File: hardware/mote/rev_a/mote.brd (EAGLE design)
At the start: 160 x 100 mm, 71 parts, among them Q1 CSD22206W, Q2 CSD75207W15, Q3 CSD75207W15, Q4 CSD13303W1015, Q5 CSD22206W, U1 NRF52840, U10 MS5637-02BA03, U3 MAX17222, U4 TPS3839G25DBZ, U5 SI7021-A20-GM1, U6 ISL29125, U7 MAX44009, U8 LIS2DW12, U9 AB1815-T3, X1 7V-32.000MAHV-T, X3 ABS07-32.768KHZ-7-T

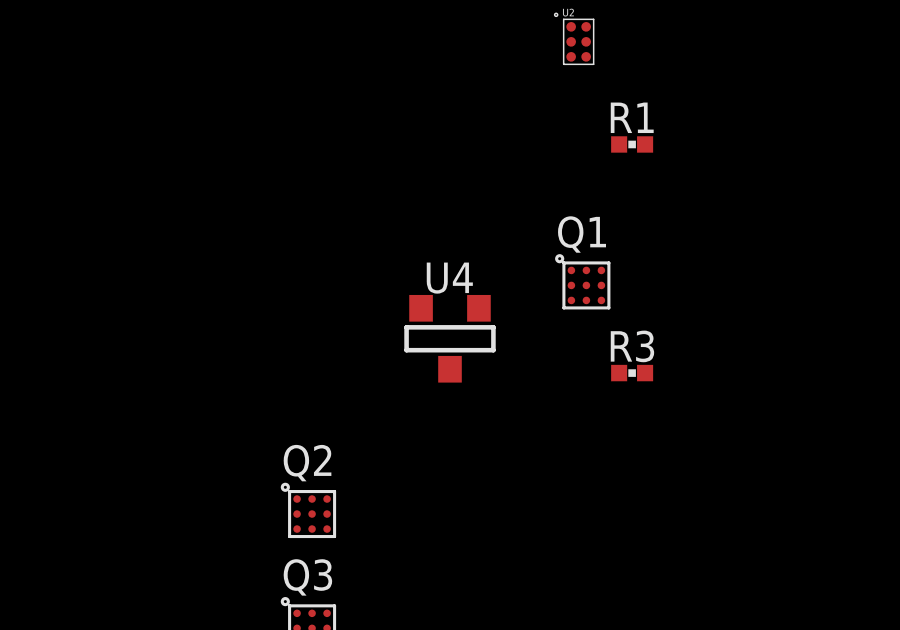
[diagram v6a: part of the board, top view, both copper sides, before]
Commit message: Do undervoltage check in software
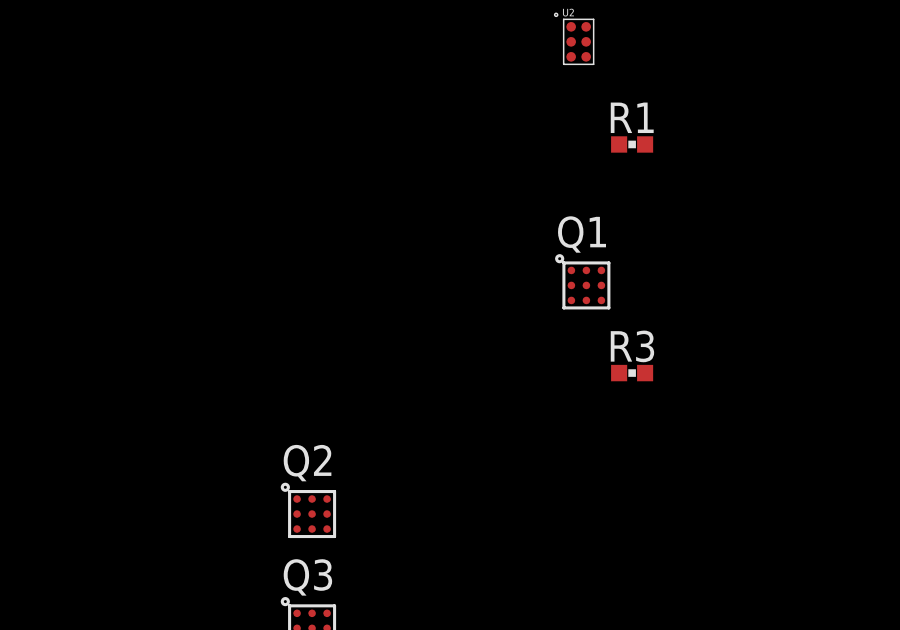
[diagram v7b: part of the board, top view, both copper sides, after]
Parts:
- removed U4: TPS3839G25DBZ, chips:SOT-23
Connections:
- removed net N$15: D3.A, Q4.A2, Q5.A1, R6.1, TP3.TESTPOINT, U4.2
- new net SRC_SW: D3.A, Q4.A2, Q5.A1, R6.1, TP3.TESTPOINT
- net GND: no longer U4.1
- net N$24: no longer U4.3
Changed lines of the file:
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@@
 " x="0.762" y="-40.513" size="1.778" layer="27" display="off"/>
-</element>
-<element name="U4" library="chips" package="SOT-23" value="TPS3839G25DBZ" x="-5.334" y="-39.37">
-<attribute name="DIGIKEY" value="296-42522-1-ND" x="-5.334" y="-39.37" size="1.778" layer="27" display="off"/>
-<attribute name="MANUFACTURER" value="TEXAS INSTRUMENTS" x="-5.334" y="-39.37" size="1.778" layer="27" display="off"/>
-<attribute name="MPN" value="TPS3839G25DBZR" x="-5.334" y="-39.37" size="1.778" layer="27" display="off"/>
 </element>
 <element name="Q2" library="fets" package="DSBGA" value="CSD75207W15" x="-9.906" y="-45.212">
@@
 <via x="33.147" y="21.717" extent="1-16" drill="0.762"/>
 <via x="26.797" y="15.621" extent="1-16" drill="0.762"/>
-<contactref element="U4" pad="1"/>
 <contactref element="Q4" pad="C2"/>
 <contactref element="Q4" pad="B2"/>
@@
 <wire x1="-9.402" y1="-53.332" x2="-70.525" y2="-89.4" width="0" layer="19" extent="1-1"/>
 <wire x1="-9.402" y1="-52.832" x2="-9.402" y2="-53.332" width="0" layer="19" extent="1-1"/>
-<wire x1="-4.3434" y1="-38.354" x2="-9.402" y2="-52.832" width="0" layer="19" extent="1-1"/>
-<wire x1="0.32893125" y1="-40.513" x2="-4.3434" y2="-38.354" width="0" layer="19" extent="1-1"/>
-<wire x1="-0.77" y1="-29.472" x2="-4.3434" y2="-38.354" width="0" layer="19" extent="1-1"/>
+<wire x1="0.32893125" y1="-40.513" x2="-9.402" y2="-52.832" width="0" layer="19" extent="1-1"/>
+<wire x1="-0.77" y1="-29.472" x2="0.32893125" y2="-40.513" width="0" layer="19" extent="1-1"/>
 <wire x1="-0.77" y1="-28.972" x2="-0.77" y2="-29.472" width="0" layer="19" extent="1-1"/>
 <wire x1="15.43" y1="-22.86" x2="-0.77" y2="-28.972" width="0" layer="19" extent="1-1"/>
@@
 <wire x1="-0.77" y1="-29.972" x2="0.32893125" y2="-32.893" width="0" layer="19" extent="1-1"/>
 </signal>
-<signal name="N$15">
-<contactref element="U4" pad="2"/>
+<signal name="SRC_SW">
 <contactref element="Q5" pad="A1"/>
 <contactref element="Q4" pad="A2"/>
@@
 <wire x1="-10.406" y1="-56.142" x2="-75.36306875" y2="-93.98" width="0" layer="19" extent="1-1"/>
 <wire x1="-9.402" y1="-52.332" x2="-10.406" y2="-56.142" width="0" layer="19" extent="1-1"/>
-<wire x1="-6.2738" y1="-38.354" x2="-9.402" y2="-52.332" width="0" layer="19" extent="1-1"/>
-<wire x1="-56.261" y1="61.722" x2="-6.2738" y2="-38.354" width="0" layer="19" extent="1-1"/>
+<wire x1="-56.261" y1="61.722" x2="-9.402" y2="-52.332" width="0" layer="19" extent="1-1"/>
 </signal>
 <signal name="N$17">
@@
 <contactref element="Q1" pad="C2"/>
 <contactref element="Q1" pad="C3"/>
-<contactref element="U4" pad="3"/>
 <contactref element="TP1" pad="TESTPOINT"/>
 <contactref element="Q5" pad="A2"/>
@@
 <wire x1="-9.406" y1="-44.712" x2="-9.406" y2="-45.212" width="0" layer="19" extent="1-1"/>
 <wire x1="-9.906" y1="-44.712" x2="-9.406" y2="-44.712" width="0" layer="19" extent="1-1"/>
-<wire x1="-5.3086" y1="-40.386" x2="-9.406" y2="-44.712" width="0" layer="19" extent="1-1"/>
-<wire x1="-1.262" y1="-38.092" x2="-5.3086" y2="-40.386" width="0" layer="19" extent="1-1"/>
+<wire x1="-1.262" y1="-38.092" x2="-9.406" y2="-44.712" width="0" layer="19" extent="1-1"/>
 <wire x1="-0.762" y1="-38.092" x2="-1.262" y2="-38.092" width="0" layer="19" extent="1-1"/>
 <wire x1="-0.262" y1="-38.092" x2="-0.762" y2="-38.092" width="0" layer="19" extent="1-1"/>

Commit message: Connect all gpio, add pir
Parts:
- added J1: TC2030-JLINK-L, connector:TC2030-IDC
- added JP1, JP2, JP3, JP4, JP5, JP6, JP7, JP8: (no value), SparkFun-Passives:SJ_2S
- added Q10, Q11, Q6, Q7, Q8, Q9: CSD22206W, fets:DSBGA
- added R10, R11, R12, R13, R14, R9: 100MΩ, passives:0402_RES
- added TP12, TP13, TP14, TP15, TP16, TP17, TP18, TP19, TP20, TP21, TP22, TP23, TP24, TP25, TP26, TP27, TP28, TP29: TEST_POINT_0.040IN, headers:TESTPOINT_0.040IN
- added U4: AMN41121, chips:AMN2
- R1: value 1k -> 1kΩ
- R2: value 80.6k -> 80.6kΩ
- R3: value 20 -> 20Ω
- R4: value 33M -> 33MΩ
- R5, R6: value 100k -> 100kΩ
- R7, R8: value 10k -> 10kΩ
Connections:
- removed net !LGHT_INT: U7.4
- removed net ACL_CS: U8.2
- removed net ACL_INT1: U8.12
- removed net ACL_INT2: U8.11
- removed net CS_RTC: U9.12
- removed net ENABLE: R4.2
- removed net SW1: L3.P$2, TP11.TESTPOINT, U3.2
- new net !ACC_EN: Q6.A1, R9.1, U1.A14
- new net !CLR_EN: Q7.A1, R10.1, U1.B15
- new net !HUM_EN: Q10.A1, R13.1, U1.B19
- new net !LT_EN: Q8.A1, R11.1, U1.A16
- new net !LT_INT: U1.U24, U7.4
- new net !PIR_EN: Q11.A1, R14.1, U1.A20
- new net !PR_EN: Q9.A1, R12.1, U1.B17
- new net ACC_CS: U1.AD12, U8.2
- new net ACC_INT1: U1.R24, U8.12
- new net ACC_INT2: U1.P23, U8.11
- new net N$15: C17.1, C9.1, Q6.A2, Q6.A3, Q6.B1, Q6.B2, Q6.B3, U8.10, U8.9
- new net N$19: C10.1, C20.1, Q7.A2, Q7.A3, Q7.B1, Q7.B2, Q7.B3, U6.1
- new net N$20: C21.1, Q8.A2, Q8.A3, Q8.B1, Q8.B2, Q8.B3, U7.1
- new net N$21: C18.1, Q9.A2, Q9.A3, Q9.B1, Q9.B2, Q9.B3, U10.1
- new net N$22: C19.1, Q10.A2, Q10.A3, Q10.B1, Q10.B2, Q10.B3, U5.5
- new net N$23: Q11.A2, Q11.A3, Q11.B1, Q11.B2, Q11.B3, U4.VCC
- new net N$28: J1.2, U1.AC24
- new net N$29: J1.4, U1.AA24
- new net N$33: JP2.1, Q7.C1, Q7.C2, Q7.C3, R10.2, TP14.TESTPOINT
- new net N$34: JP3.1, Q8.C1, Q8.C2, Q8.C3, R11.2, TP16.TESTPOINT
- new net N$35: JP4.1, Q9.C1, Q9.C2, Q9.C3, R12.2, TP18.TESTPOINT
- new net N$36: JP5.1, Q10.C1, Q10.C2, Q10.C3, R13.2, TP20.TESTPOINT
- new net N$37: JP1.1, Q6.C1, Q6.C2, Q6.C3, R9.2, TP12.TESTPOINT
- new net N$39: C12.1, C14.1, C6.1, C7.1, C8.1, JP7.1, TP24.TESTPOINT, U1.A22, U1.AD14, U1.AD23, U1.B1, U1.W1, U1.Y2
- new net N$42: C25.1, JP6.1, TP22.TESTPOINT, U9.13
- new net N$43: JP6.2, TP23.TESTPOINT
- new net PIR_OUT: U1.R1, U1.V23, U4.OUT
- new net RTC_CS: U1.AC11, U9.12
- new net SW: L3.P$2, TP11.TESTPOINT, U1.AD20, U3.2
- net !CLR_INT: now also U1.T23
- net GND: now also J1.5, TP26.TESTPOINT, TP27.TESTPOINT, U4.GND
- net MISO: now also U1.AD10
- net MOSI: now also U1.AC9
- net N$24: now also JP8.1, Q11.C1, Q11.C2, Q11.C3, R14.2, TP28.TESTPOINT; no longer BAT1.+, D1.+, Q1.C1, Q1.C2, Q1.C3, Q2.A2, Q2.A3, Q2.B3, Q5.A2, Q5.A3, Q5.B1, Q5.B2, Q5.B3, R1.2, TP1.TESTPOINT, U2.A1, U2.C1
- net SCK: now also U1.AD8
- net SCL: now also U1.H2
- net SDA: now also U1.G1
- net VBAT: now also U1.B13; no longer C25.1, U9.13
- net VCC: now also J1.1, JP1.2, JP2.2, JP3.2, JP4.2, JP5.2, JP7.2, JP8.2, TP13.TESTPOINT, TP15.TESTPOINT, TP17.TESTPOINT, TP19.TESTPOINT, TP21.TESTPOINT, TP25.TESTPOINT, TP29.TESTPOINT; no longer C10.1, C12.1, C14.1, C17.1, C18.1, C19.1, C20.1, C21.1, C6.1, C7.1, C8.1, C9.1, U1.A22, U1.AD14, U1.AD23, U1.B1, U1.W1, U1.Y2, U10.1, U5.5, U6.1, U7.1, U8.10, U8.9
- net VSW: now also BAT1.+, D1.+, Q1.C1, Q1.C2, Q1.C3, Q2.A2, Q2.A3, Q2.B3, Q5.A2, Q5.A3, Q5.B1, Q5.B2, Q5.B3, R1.2, R4.2, TP1.TESTPOINT, U1.A12, U2.A1, U2.C1
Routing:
- net SW1: track 19.2 -> 0.00 mm
- net SW: track 0.00 -> 19.2 mm
- net VCC: track 6.14 -> 0.00 mm, vias 2 -> 0
- net N$39: track 0.00 -> 6.14 mm, vias 0 -> 2
- net VSW: track 4.63 -> 7.79 mm
- net ENABLE: track 3.16 -> 0.00 mm
- added copper zone on layer 1, net SW
- removed copper zone on layer 1, net SW1
